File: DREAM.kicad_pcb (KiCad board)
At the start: 2 copper layers, 100 x 60 mm, 137 parts, among them J401 KLDX-0202-B, J402 EBWA-02-B, J501 Conn_ST_STDC14, J502 USB4105-GF-A, J601 1-1337535-0, J602 1-1337535-0, J603 1-1337535-0, J701 PH1-02-UA, Q401 MCU18P10Y-TP, SW501 PTS526SK15SMTR2 LFS, U401 TPS7A2030PDBVR, U501 STM32G441KBT6, U502 USBLC6-2SC6, U601 TSV912AIDR, U602 TSV912AIDR, U603 LM358LVIDR, U604 TSV912AIDR, U605 TSV912AIDR, U701 LM358LVIDR, U702 LM358LVIDR, Y501 ATS08A-E

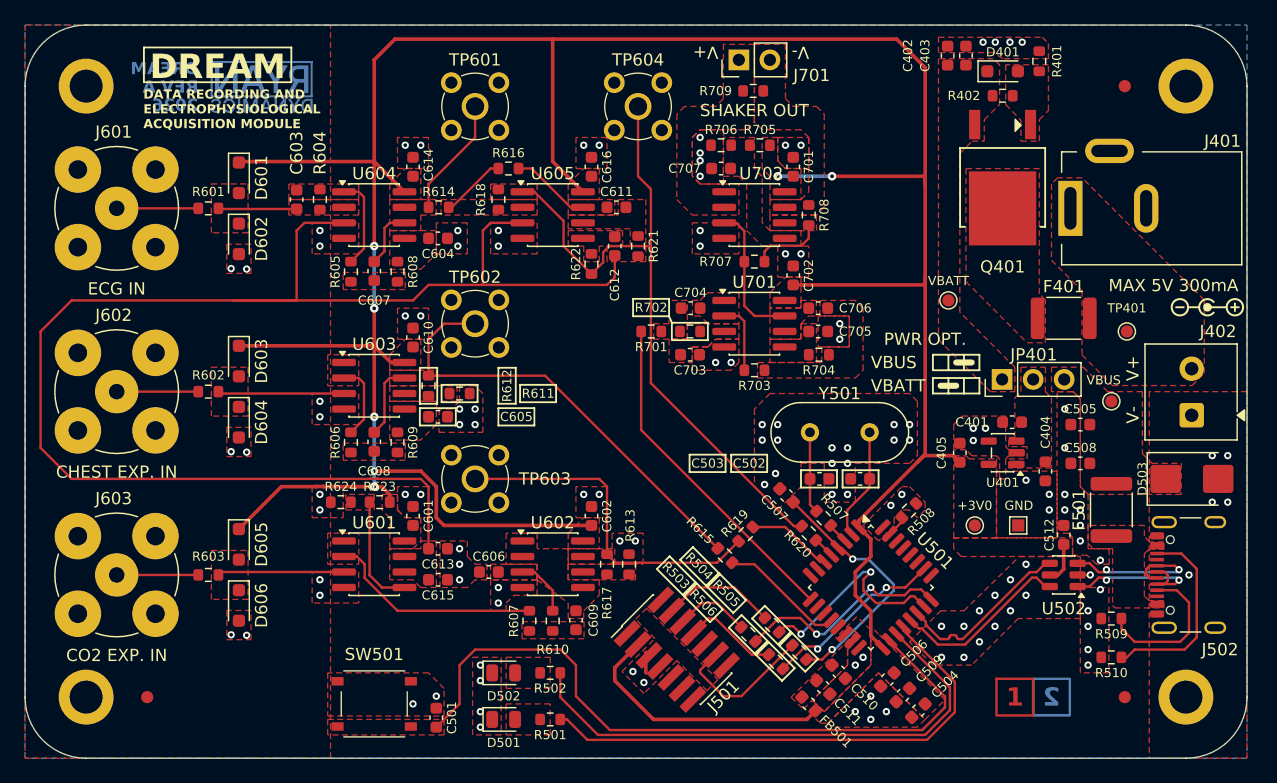
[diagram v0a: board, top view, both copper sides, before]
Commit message: fix: net naming, NC STM32 pins, silkscreen, pin 1 indicator
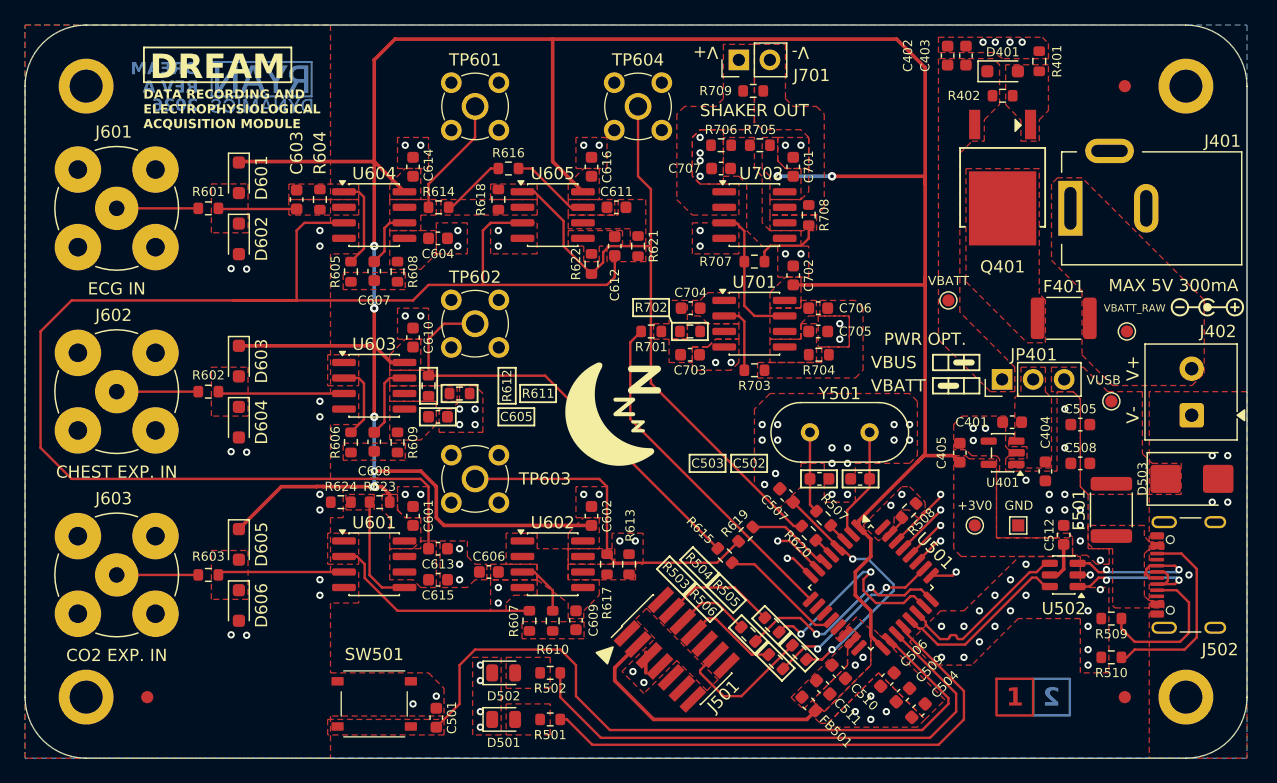
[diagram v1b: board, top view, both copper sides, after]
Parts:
- TP501: value VBUS -> VUSB
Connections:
- net /ARCHITECTURE/DIGITAL AND HMI/VBUS_RAW renamed /ARCHITECTURE/DIGITAL AND HMI/VBUS
- net VBUS renamed VUSB
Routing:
- net unconnected-(U501-PB7-Pad30): track 0.00 -> 5.32 mm, vias 0 -> 1
- net unconnected-(U501-PB6-Pad29): track 0.00 -> 4.52 mm, vias 0 -> 1
- net unconnected-(U501-PA2-Pad7): track 0.00 -> 4.19 mm, vias 0 -> 1
- net unconnected-(U501-PB5-Pad28): track 0.00 -> 3.48 mm, vias 0 -> 1
- net unconnected-(U501-PB4-Pad27): track 0.00 -> 2.62 mm, vias 0 -> 1
- net unconnected-(U501-PA3-Pad8): track 0.00 -> 2.49 mm, vias 0 -> 1
- net unconnected-(U501-PA15-Pad25): track 0.00 -> 2.18 mm, vias 0 -> 1
- net /ARCHITECTURE/DIGITAL AND HMI/LED_GRN: track 42.6 -> 44.4 mm
- net /ARCHITECTURE/DIGITAL AND HMI/LED_RED: track 44.0 -> 45.0 mm
- net /ARCHITECTURE/ANALOGUE OUTPUTS/DAC_SHAKER: track 27.7 -> 28.4 mm
